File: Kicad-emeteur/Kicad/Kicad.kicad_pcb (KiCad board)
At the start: 4 copper layers, 32.1 x 28.8 mm, 28 parts, among them J1 Conn_02x07_Odd_Even, J2 USB_C_Receptacle_PowerOnly_6P, J5 Conn_01x02, J52 Conn_01x04, J6 Conn_01x03, J62 Conn_01x03, U1 STM32L021K4Tx, U2 BU33SD5WG-TR

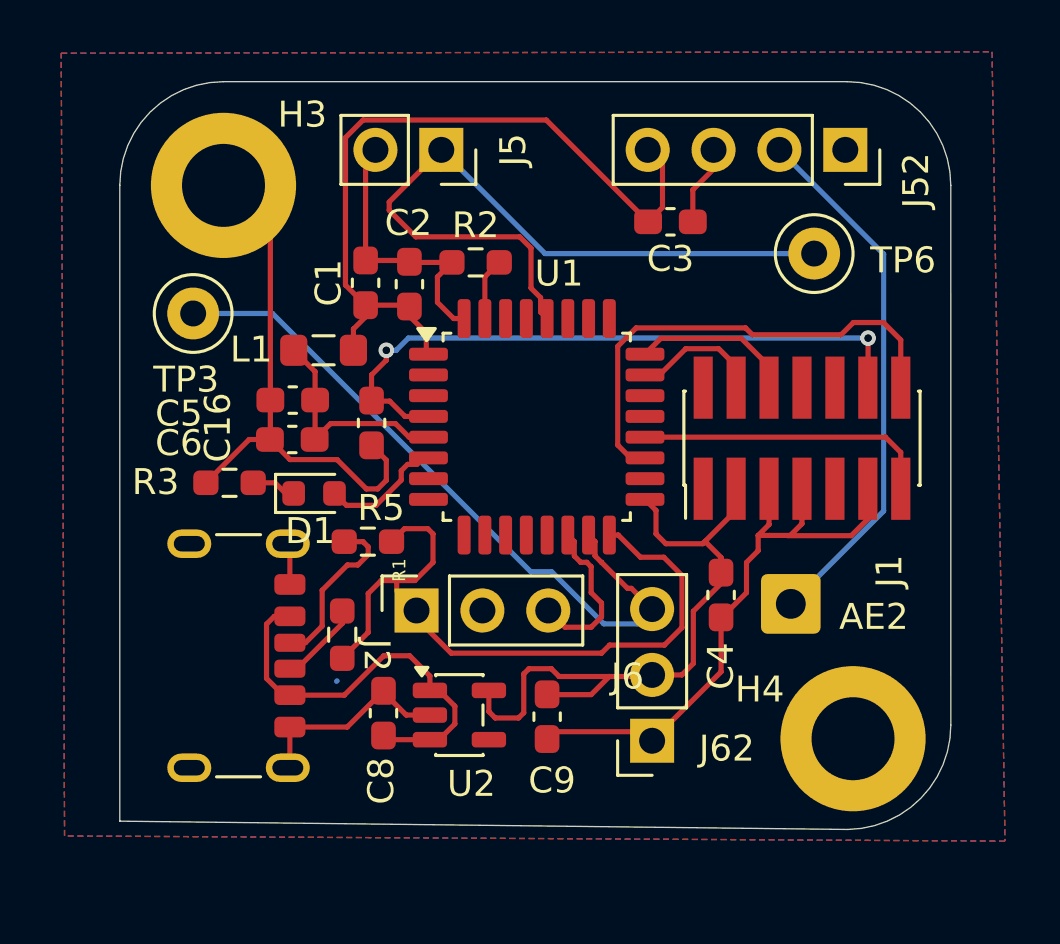
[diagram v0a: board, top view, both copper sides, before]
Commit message: feat: Add initial Kicad PCB designs for receiver and emitter, and generate emitter Gerber files.
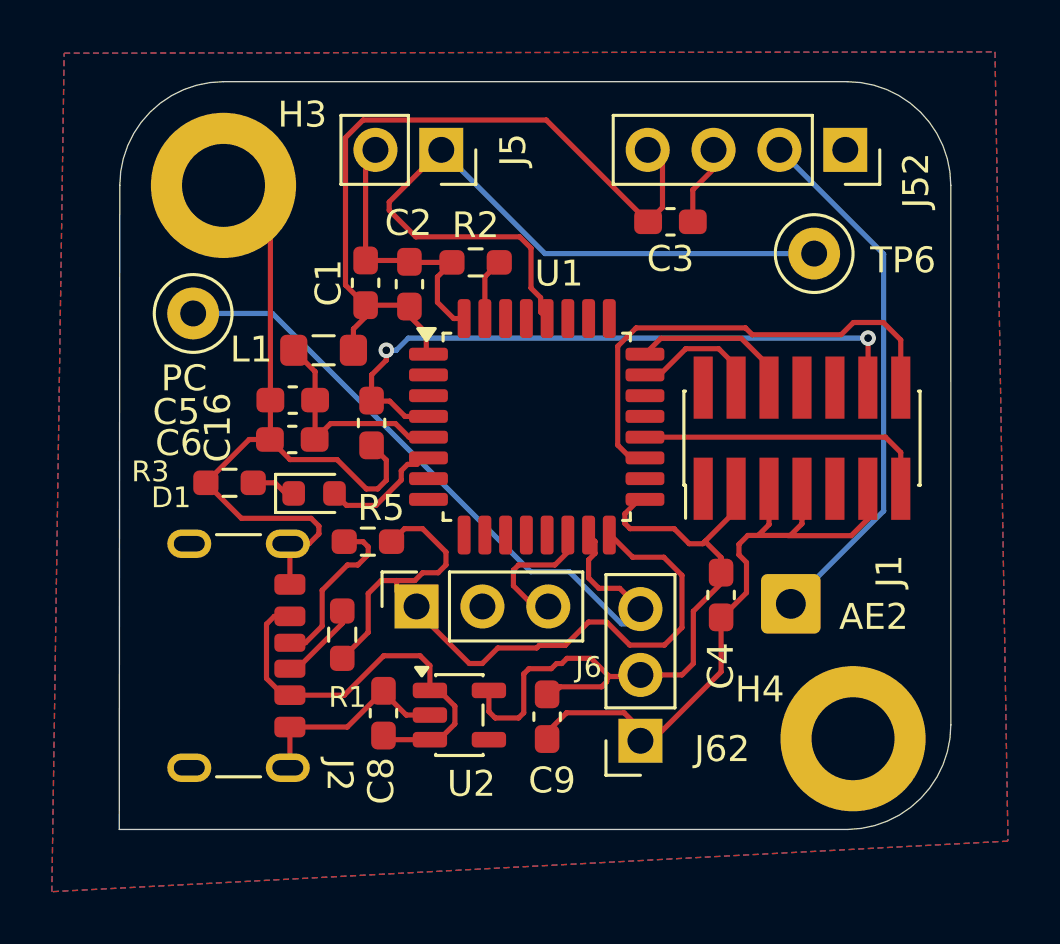
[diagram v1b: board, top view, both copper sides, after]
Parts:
- moved J62 0.45 mm to (115.6, 118.4)
- moved J6 0.16 mm to (106.9, 113.2)
- renumbered TP3 to PC
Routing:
- net GND: track 98.0 -> 107.4 mm
- net +3.3V: track 54.5 -> 56.1 mm
- net PL: track 6.32 -> 5.32 mm
- net PC: track 26.9 -> 27.7 mm
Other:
- outline, holes or cut-outs redrawn
